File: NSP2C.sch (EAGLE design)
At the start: 21 parts, among them Q1 600mA/40V, Q2 IRF540

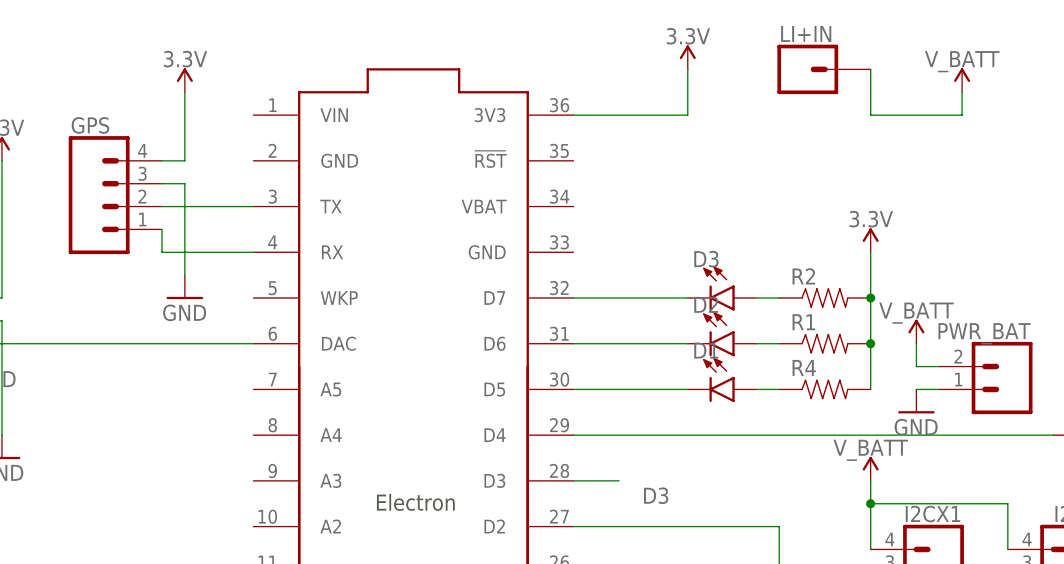
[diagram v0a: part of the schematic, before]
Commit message: Added routes to PCB in 1 Lauyer (VC)
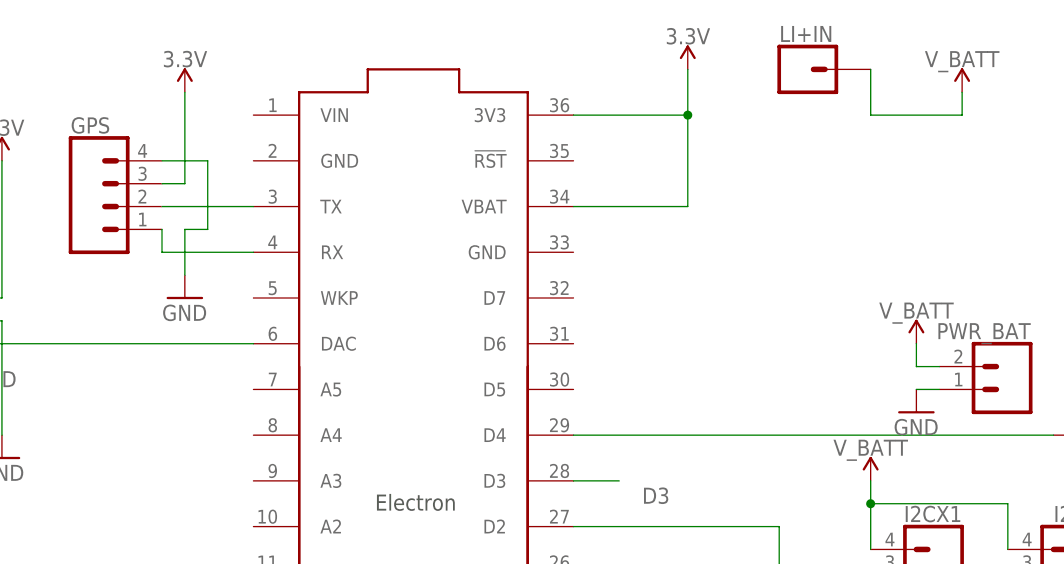
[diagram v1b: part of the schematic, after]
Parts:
- removed D1, D2, D3: (no value), SparkFun-LED:LED-3MM-NO_SILK
- removed R1, R2, R4: (no value), SparkFun-Passives:RESISTORPTH-1/6W
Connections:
- removed net N$2 (its old number): D3.C, U$1.D7
- removed net N$3: D2.C, U$1.D6
- removed net N$4: D1.C, U$1.D5
- removed net N$5: D2.A, R1.1
- removed net N$7: D3.A, R2.1
- removed net N$8: D1.A, R4.1
- net 3.3V: now also GPS.3, U$1.VBAT; no longer GPS.4, R1.2, R2.2, R4.2
- net GND: now also GPS.4; no longer GPS.3
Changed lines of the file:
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@@
 <part name="PWR_BAT" library="SparkFun-Connectors" deviceset="CONN_02" device=""/>
 <part name="GPS" library="SparkFun-Connectors" deviceset="CONN_04" device=""/>
-<part name="R1" library="SparkFun-Passives" deviceset="RESISTOR" device="PTH-1/6W"/>
-<part name="D1" library="SparkFun-LED" deviceset="LED" device="-3MM-NO_SILK"/>
 <part name="SUPPLY3" library="SparkFun-PowerSymbols" deviceset="3.3V" device=""/>
 <part name="LI+IN" library="SparkFun-Connectors" deviceset="CONN_01" device=""/>
@@
 <part name="IRIDIUM" library="SparkFun-Connectors" deviceset="CONN_05" device=""/>
 <part name="GND2" library="supply1" library_urn="urn:adsk.eagle:library:371" deviceset="GND" device=""/>
-<part name="D2" library="SparkFun-LED" deviceset="LED" device="-3MM-NO_SILK"/>
-<part name="D3" library="SparkFun-LED" deviceset="LED" device="-3MM-NO_SILK"/>
-<part name="SUPPLY5" library="SparkFun-PowerSymbols" deviceset="3.3V" device=""/>
 <part name="GND3" library="supply1" library_urn="urn:adsk.eagle:library:371" deviceset="GND" device=""/>
 <part name="LI+2" library="SparkFun-PowerSymbols" deviceset="V_BATT" device=""/>
@@
 <part name="SUPPLY1" library="SparkFun-PowerSymbols" deviceset="3.3V" device=""/>
 <part name="GND6" library="supply1" library_urn="urn:adsk.eagle:library:371" deviceset="GND" device=""/>
-<part name="R2" library="SparkFun-Passives" deviceset="RESISTOR" device="PTH-1/6W"/>
-<part name="R4" library="SparkFun-Passives" deviceset="RESISTOR" device="PTH-1/6W"/>
 <part name="HEATPADS" library="SparkFun-Connectors" deviceset="CONN_04" device=""/>
 <part name="Q2" library="transistor-fet" library_urn="urn:adsk.eagle:library:396" deviceset="IRF540" device="" package3d_urn="urn:adsk.eagle:package:28520/1"/>
@@
 <instance part="PWR_BAT" gate="G$1" x="124.46" y="60.96" rot="MR0"/>
 <instance part="GPS" gate="G$1" x="25.4" y="81.28"/>
-<instance part="R1" gate="G$1" x="104.14" y="66.04"/>
-<instance part="D1" gate="G$1" x="93.98" y="60.96" rot="R270"/>
 <instance part="SUPPLY3" gate="G$1" x="88.9" y="96.52"/>
 <instance part="LI+IN" gate="G$1" x="101.6" y="96.52"/>
@@
 <instance part="IRIDIUM" gate="G$1" x="124.46" y="12.7" rot="MR0"/>
 <instance part="GND2" gate="1" x="104.14" y="30.48"/>
-<instance part="D2" gate="G$1" x="93.98" y="66.04" rot="R270"/>
-<instance part="D3" gate="G$1" x="93.98" y="71.12" rot="R270"/>
-<instance part="SUPPLY5" gate="G$1" x="109.22" y="76.2"/>
 <instance part="GND3" gate="1" x="114.3" y="58.42"/>
 <instance part="LI+2" gate="G$1" x="114.3" y="66.04"/>
@@
 <instance part="SUPPLY1" gate="G$1" x="12.7" y="86.36"/>
 <instance part="GND6" gate="1" x="12.7" y="53.34"/>
-<instance part="R2" gate="G$1" x="104.14" y="71.12"/>
-<instance part="R4" gate="G$1" x="104.14" y="60.96"/>
 <instance part="HEATPADS" gate="G$1" x="210.82" y="43.18" rot="MR0"/>
 <instance part="Q2" gate="G$1" x="185.42" y="43.18"/>
@@
 <net name="3.3V" class="0">
 <segment>
-<pinref part="GPS" gate="G$1" pin="4"/>
-<wire x1="30.48" y1="86.36" x2="33.02" y2="86.36" width="0.1524" layer="91"/>
-<pinref part="SUPPLY4" gate="G$1" pin="3.3V"/>
-<wire x1="33.02" y1="86.36" x2="33.02" y2="93.98" width="0.1524" layer="91"/>
-</segment>
-<segment>
 <pinref part="U$1" gate="G$1" pin="3V3"/>
 <wire x1="76.2" y1="91.44" x2="88.9" y2="91.44" width="0.1524" layer="91"/>
 <pinref part="SUPPLY3" gate="G$1" pin="3.3V"/>
 <wire x1="88.9" y1="91.44" x2="88.9" y2="96.52" width="0.1524" layer="91"/>
-</segment>
-<segment>
-<pinref part="R1" gate="G$1" pin="2"/>
-<pinref part="SUPPLY5" gate="G$1" pin="3.3V"/>
-<wire x1="109.22" y1="76.2" x2="109.22" y2="71.12" width="0.1524" layer="91"/>
-<pinref part="R4" gate="G$1" pin="2"/>
-<wire x1="109.22" y1="71.12" x2="109.22" y2="66.04" width="0.1524" layer="91"/>
-<wire x1="109.22" y1="60.96" x2="109.22" y2="66.04" width="0.1524" layer="91"/>
-<junction x="109.22" y="66.04"/>
-<pinref part="R2" gate="G$1" pin="2"/>
-<junction x="109.22" y="71.12"/>
+<wire x1="88.9" y1="91.44" x2="88.9" y2="81.28" width="0.1524" layer="91"/>
+<junction x="88.9" y="91.44"/>
+<pinref part="U$1" gate="G$1" pin="VBAT"/>
+<wire x1="88.9" y1="81.28" x2="76.2" y2="81.28" width="0.1524" layer="91"/>
 </segment>
 <segment>
@@
 <pinref part="SUPPLY1" gate="G$1" pin="3.3V"/>
 <wire x1="12.7" y1="86.36" x2="12.7" y2="71.12" width="0.1524" layer="91"/>
+</segment>
+<segment>
+<pinref part="SUPPLY4" gate="G$1" pin="3.3V"/>
+<wire x1="33.02" y1="83.82" x2="33.02" y2="93.98" width="0.1524" layer="91"/>
+<pinref part="GPS" gate="G$1" pin="3"/>
+<wire x1="33.02" y1="83.82" x2="30.48" y2="83.82" width="0.1524" layer="91"/>
 </segment>
 </net>
@@
 </segment>
 <segment>
-<pinref part="GPS" gate="G$1" pin="3"/>
 <pinref part="GND8" gate="1" pin="GND"/>
-<wire x1="30.48" y1="83.82" x2="33.02" y2="83.82" width="0.1524" layer="91"/>
-<wire x1="33.02" y1="83.82" x2="33.02" y2="73.66" width="0.1524" layer="91"/>
+<wire x1="33.02" y1="73.66" x2="33.02" y2="78.74" width="0.1524" layer="91"/>
+<wire x1="33.02" y1="78.74" x2="35.56" y2="78.74" width="0.1524" layer="91"/>
+<wire x1="35.56" y1="78.74" x2="35.56" y2="86.36" width="0.1524" layer="91"/>
+<pinref part="GPS" gate="G$1" pin="4"/>
+<wire x1="35.56" y1="86.36" x2="30.48" y2="86.36" width="0.1524" layer="91"/>
 </segment>
 </net>
@@
 </segment>
 </net>
-<net name="N$2" class="0">
-<segment>
-<pinref part="U$1" gate="G$1" pin="D7"/>
-<pinref part="D3" gate="G$1" pin="C"/>
-<wire x1="76.2" y1="71.12" x2="88.9" y2="71.12" width="0.1524" layer="91"/>
-</segment>
-</net>
-<net name="N$3" class="0">
-<segment>
-<pinref part="U$1" gate="G$1" pin="D6"/>
-<pinref part="D2" gate="G$1" pin="C"/>
-<wire x1="76.2" y1="66.04" x2="88.9" y2="66.04" width="0.1524" layer="91"/>
-</segment>
-</net>
-<net name="N$4" class="0">
-<segment>
-<pinref part="U$1" gate="G$1" pin="D5"/>
-<pinref part="D1" gate="G$1" pin="C"/>
-<wire x1="76.2" y1="60.96" x2="88.9" y2="60.96" width="0.1524" layer="91"/>
-</segment>
-</net>
-<net name="N$5" class="0">
-<segment>
-<pinref part="D2" gate="G$1" pin="A"/>
-<wire x1="96.52" y1="66.04" x2="99.06" y2="66.04" width="0.1524" layer="91"/>
-<pinref part="R1" gate="G$1" pin="1"/>
-</segment>
-</net>
 <net name="UART4_RX" class="0">
 <segment>
@@
 <pinref part="BZR" gate="G$1" pin="1"/>
 <pinref part="Q1" gate="G$1" pin="C"/>
-</segment>
-</net>
-<net name="N$7" class="0">
-<segment>
-<pinref part="D3" gate="G$1" pin="A"/>
-<pinref part="R2" gate="G$1" pin="1"/>
-<wire x1="99.06" y1="71.12" x2="96.52" y2="71.12" width="0.1524" layer="91"/>
-</segment>
-</net>
-<net name="N$8" class="0">
-<segment>
-<pinref part="D1" gate="G$1" pin="A"/>
-<pinref part="R4" gate="G$1" pin="1"/>
-<wire x1="96.52" y1="60.96" x2="99.06" y2="60.96" width="0.1524" layer="91"/>
 </segment>
 </net>
@@
 <wire x1="30.48" y1="76.2" x2="30.48" y2="78.74" width="0.1524" layer="91"/>
 <pinref part="GPS" gate="G$1" pin="1"/>
-</segment>
-</net>
-<net name="N$13" class="0">
-<segment>
-<pinref part="U$1" gate="G$1" pin="TX"/>
-<pinref part="GPS" gate="G$1" pin="2"/>
-<wire x1="40.64" y1="81.28" x2="30.48" y2="81.28" width="0.1524" layer="91"/>
 </segment>
 </net>
@@
 </segment>
 </net>
+<net name="N$2" class="0">
+<segment>
+<pinref part="U$1" gate="G$1" pin="TX"/>
+<pinref part="GPS" gate="G$1" pin="2"/>
+<wire x1="40.64" y1="81.28" x2="30.48" y2="81.28" width="0.1524" layer="91"/>
+</segment>
+</net>

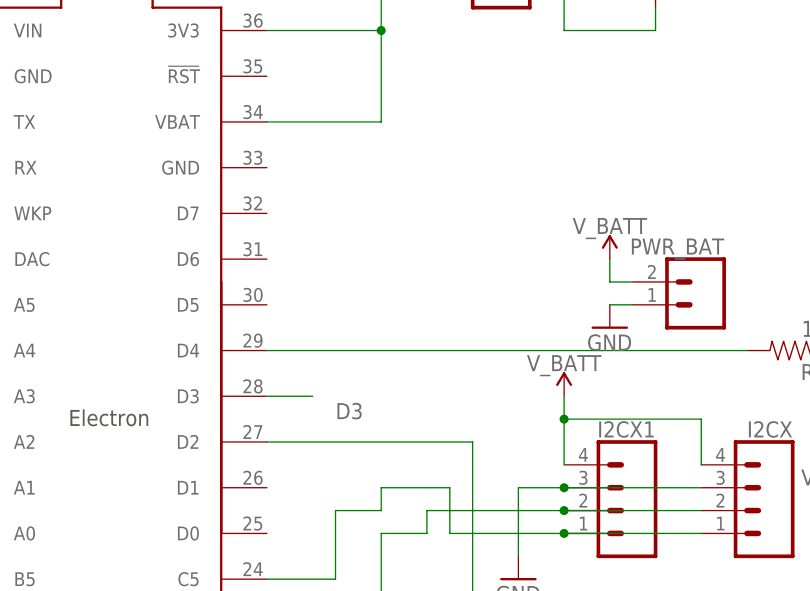
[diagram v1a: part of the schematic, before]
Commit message: Improved routing
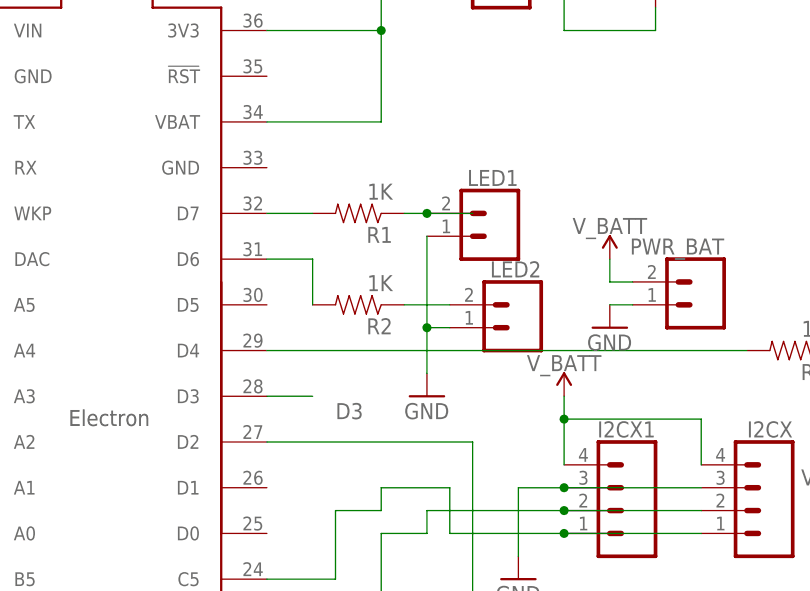
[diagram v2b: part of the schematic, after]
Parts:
- added LED1, LED2: (no value), SparkFun-Connectors:CONN_02
- added R1, R2: 1K, SparkFun-Passives:RESISTORPTH-1/6W
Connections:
- new net N$13: R2.2, U$1.D6
- new net N$16: LED2.2, R2.1
- new net N$3: R1.2, U$1.D7
- new net N$8: LED1.2, R1.1
- net GND: now also LED1.1, LED2.1
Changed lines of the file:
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@@
 <part name="R5" library="SparkFun-Passives" deviceset="RESISTOR" device="PTH-1/6W" value="10K"/>
 <part name="GND8" library="supply1" library_urn="urn:adsk.eagle:library:371" deviceset="GND" device=""/>
+<part name="R1" library="SparkFun-Passives" deviceset="RESISTOR" device="PTH-1/6W" value="1K"/>
+<part name="GND9" library="supply1" library_urn="urn:adsk.eagle:library:371" deviceset="GND" device=""/>
+<part name="LED1" library="SparkFun-Connectors" deviceset="CONN_02" device=""/>
+<part name="LED2" library="SparkFun-Connectors" deviceset="CONN_02" device=""/>
+<part name="R2" library="SparkFun-Passives" deviceset="RESISTOR" device="PTH-1/6W" value="1K"/>
 </parts>
 <sheets>
@@
 <instance part="R5" gate="G$1" x="177.8" y="33.02" rot="R270"/>
 <instance part="GND8" gate="1" x="33.02" y="71.12"/>
+<instance part="R1" gate="G$1" x="86.36" y="71.12" rot="R180"/>
+<instance part="GND9" gate="1" x="93.98" y="50.8"/>
+<instance part="LED1" gate="G$1" x="101.6" y="68.58" rot="MR0"/>
+<instance part="LED2" gate="G$1" x="104.14" y="58.42" rot="MR0"/>
+<instance part="R2" gate="G$1" x="86.36" y="60.96" rot="R180"/>
 </instances>
 <busses>
@@
 <pinref part="GPS" gate="G$1" pin="4"/>
 <wire x1="35.56" y1="86.36" x2="30.48" y2="86.36" width="0.1524" layer="91"/>
+</segment>
+<segment>
+<pinref part="LED1" gate="G$1" pin="1"/>
+<pinref part="GND9" gate="1" pin="GND"/>
+<wire x1="93.98" y1="68.58" x2="93.98" y2="58.42" width="0.1524" layer="91"/>
+<pinref part="LED2" gate="G$1" pin="1"/>
+<wire x1="93.98" y1="58.42" x2="93.98" y2="53.34" width="0.1524" layer="91"/>
+<wire x1="96.52" y1="58.42" x2="93.98" y2="58.42" width="0.1524" layer="91"/>
+<junction x="93.98" y="58.42"/>
 </segment>
 </net>
@@
 </segment>
 </net>
+<net name="N$3" class="0">
+<segment>
+<pinref part="U$1" gate="G$1" pin="D7"/>
+<pinref part="R1" gate="G$1" pin="2"/>
+<wire x1="81.28" y1="71.12" x2="76.2" y2="71.12" width="0.1524" layer="91"/>
+</segment>
+</net>
+<net name="N$8" class="0">
+<segment>
+<pinref part="R1" gate="G$1" pin="1"/>
+<wire x1="91.44" y1="71.12" x2="93.98" y2="71.12" width="0.1524" layer="91"/>
+<pinref part="LED1" gate="G$1" pin="2"/>
+<wire x1="93.98" y1="71.12" x2="99.06" y2="71.12" width="0.1524" layer="91"/>
+<junction x="93.98" y="71.12"/>
+</segment>
+</net>
+<net name="N$13" class="0">
+<segment>
+<pinref part="U$1" gate="G$1" pin="D6"/>
+<wire x1="76.2" y1="66.04" x2="81.28" y2="66.04" width="0.1524" layer="91"/>
+<pinref part="R2" gate="G$1" pin="2"/>
+<wire x1="81.28" y1="66.04" x2="81.28" y2="60.96" width="0.1524" layer="91"/>
+</segment>
+</net>
+<net name="N$16" class="0">
+<segment>
+<pinref part="R2" gate="G$1" pin="1"/>
+<pinref part="LED2" gate="G$1" pin="2"/>
+<wire x1="91.44" y1="60.96" x2="96.52" y2="60.96" width="0.1524" layer="91"/>
+</segment>
+</net>

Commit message: Added capacitor for batt source
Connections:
- net N$10 renamed BASE
- net N$12 renamed RX
- net N$2 renamed TX
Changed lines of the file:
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@@
 </segment>
 </net>
-<net name="N$10" class="0">
+<net name="BASE" class="0">
 <segment>
 <pinref part="R3" gate="G$1" pin="1"/>
@@
 </segment>
 </net>
-<net name="N$12" class="0">
+<net name="RX" class="0">
 <segment>
 <pinref part="U$1" gate="G$1" pin="RX"/>
@@
 </segment>
 </net>
-<net name="N$2" class="0">
+<net name="TX" class="0">
 <segment>
 <pinref part="U$1" gate="G$1" pin="TX"/>
